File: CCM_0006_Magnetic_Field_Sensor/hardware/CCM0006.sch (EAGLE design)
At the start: 31 parts, among them IC1 AD654, IC2 LM6061, IC4 AD8436, X1 22-23-2021

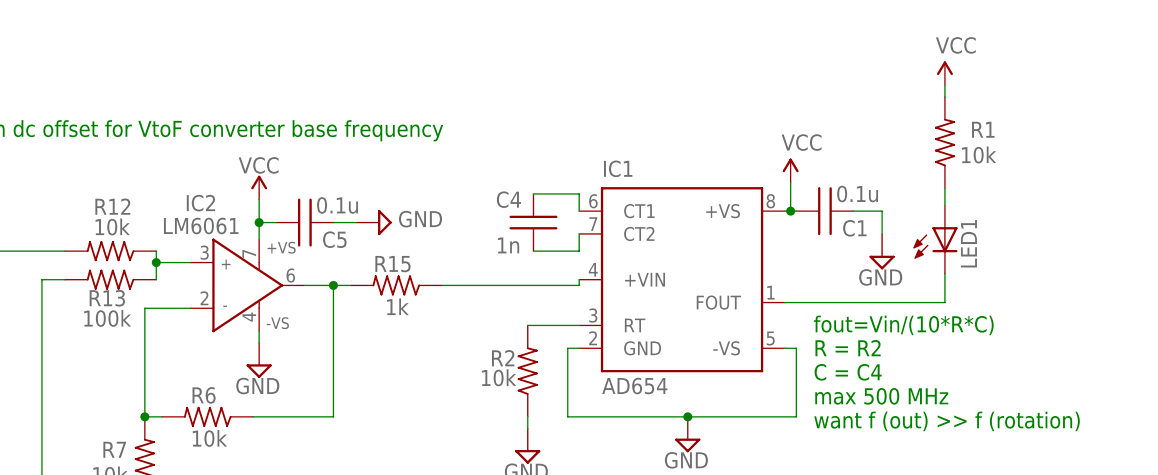
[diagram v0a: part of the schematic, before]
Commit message: added resources for updating the firmware of the reflow oven
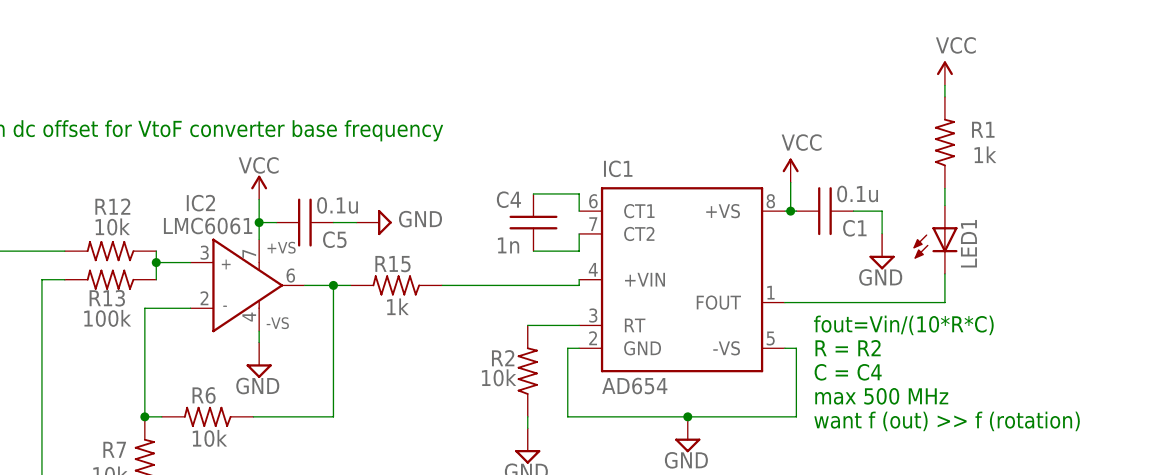
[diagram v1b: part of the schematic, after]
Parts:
- IC2: value LM6061 -> LMC6061
- R1: value 10k -> 1k
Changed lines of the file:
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@@
 <part name="IC1" library="noah" deviceset="AD654" device=""/>
 <part name="SUPPLY1" library="supply2" deviceset="AGND" device="" value="GND"/>
-<part name="R1" library="ic" deviceset="RESISTOR" device="0402" value="10k"/>
+<part name="R1" library="ic" deviceset="RESISTOR" device="0402" value="1k"/>
 <part name="P+1" library="SparkFun" deviceset="VCC" device=""/>
 <part name="P+2" library="SparkFun" deviceset="VCC" device=""/>
@@
 <part name="C7" library="ic" deviceset="CAPACITOR" device="0805" value="10u"/>
 <part name="C13" library="ic" deviceset="CAPACITOR" device="0805" value="10u"/>
-<part name="IC2" library="analog-devices" deviceset="AD820" device="R" value="LM6061"/>
+<part name="IC2" library="analog-devices" deviceset="AD820" device="R" value="LMC6061"/>
 <part name="LED1" library="led" deviceset="LED" device="3MM"/>
 <part name="C10" library="ic" deviceset="CAPACITOR" device="0402" value="0.1u"/>
